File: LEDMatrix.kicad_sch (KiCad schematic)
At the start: 50 parts, among them J1 Conn_02x04_Odd_Even, SW2 SW_Push, U1 W25Q16JVUXIQ, U2 RP2040, Y1 12.000MHz

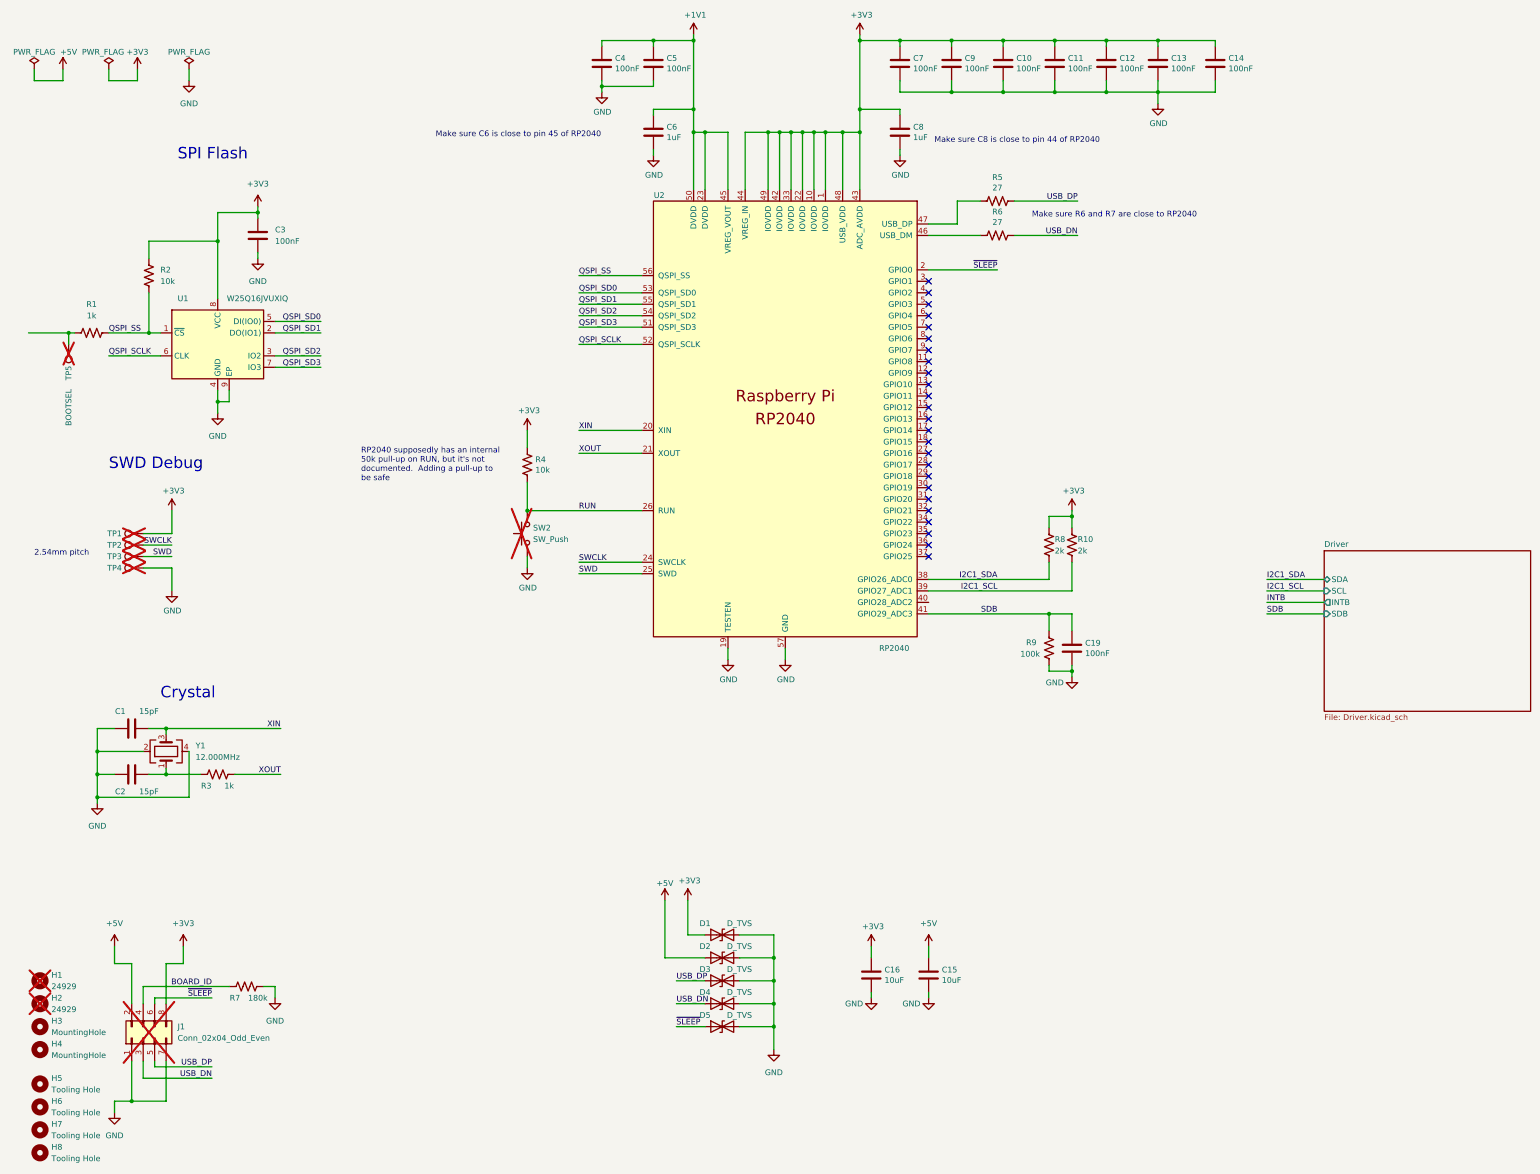
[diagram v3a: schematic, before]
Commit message: Version 2, with right angle neopixel backlighting
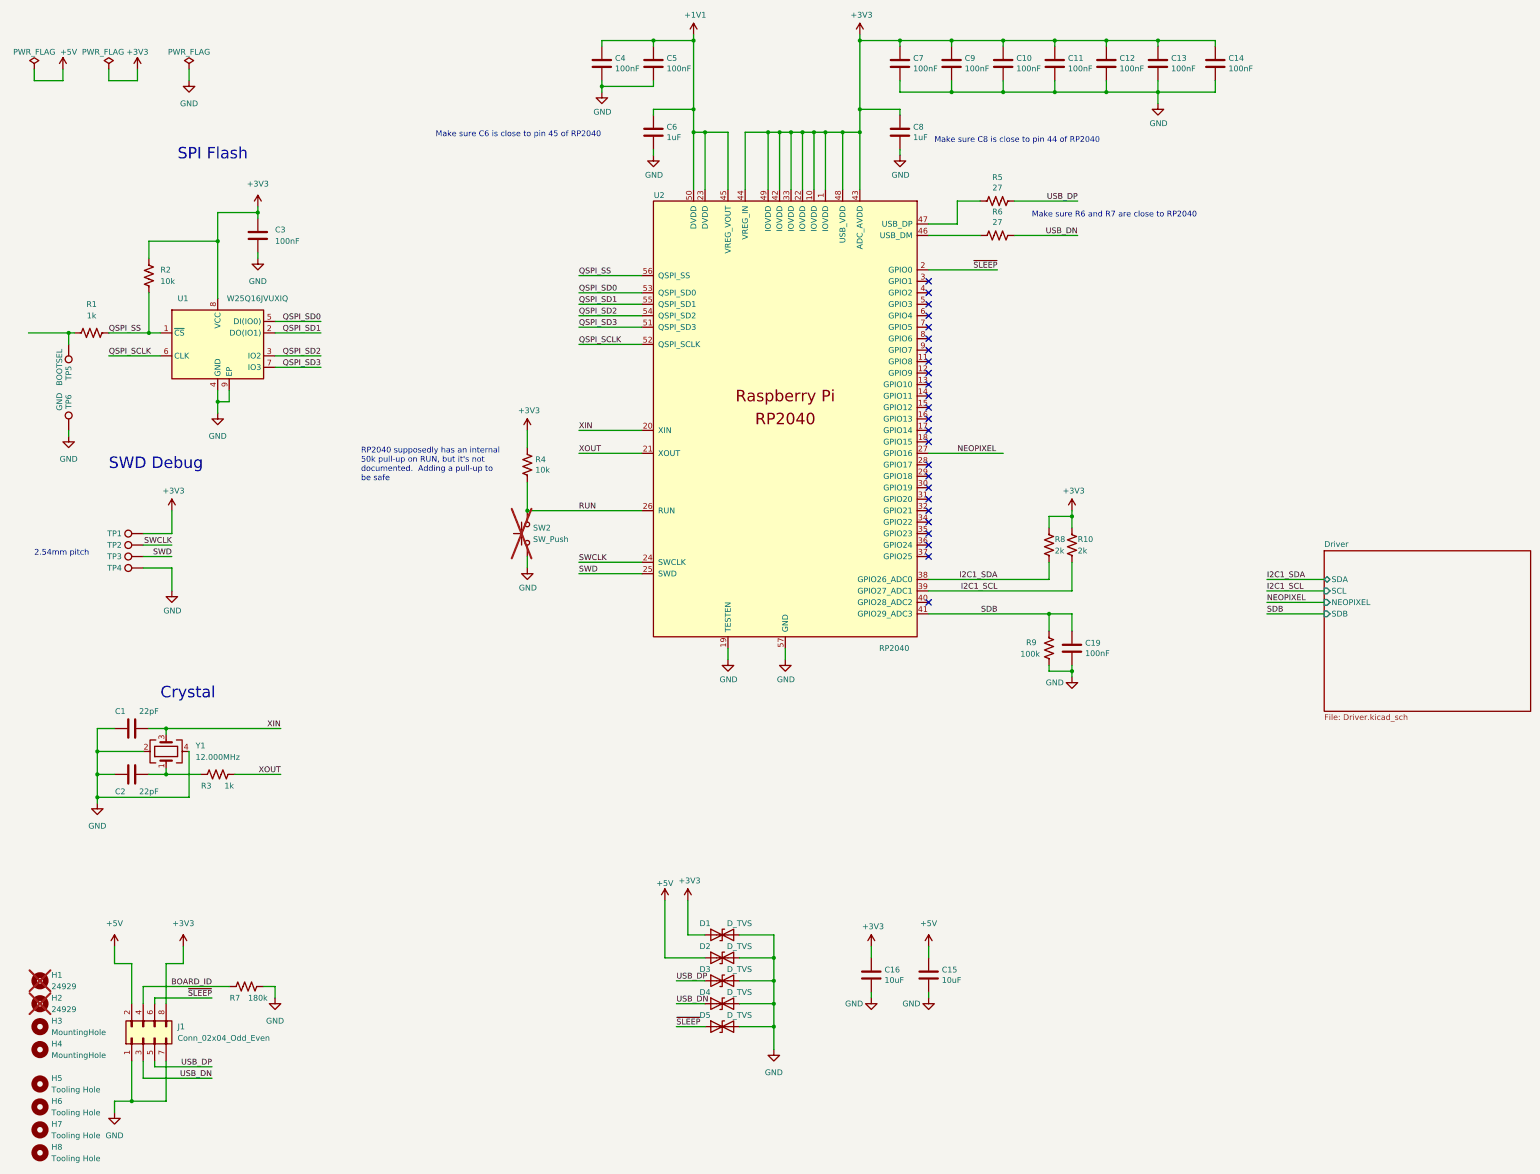
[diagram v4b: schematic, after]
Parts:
- added TP6: GND, TestPoint:TestPoint_Pad_D1.0mm, symbol Connector:TestPoint
- C1, C2: value 15pF -> 22pF
- J1, TP5: now fitted
- TP1, TP2, TP3, TP4: now fitted; now left out of the parts list
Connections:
- net GND: now also TP6.1
- net NEOPIXEL: now reaches U2.27 (GPIO16)
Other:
- sheet Driver ports: added NEOPIXEL; removed INTB
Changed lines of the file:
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@@
 	)
 	(no_connect
-		(at 224.79 113.03)
-	)
-	(no_connect
 		(at 224.79 92.71)
 	)
@@
 		(at 224.79 87.63)
 	)
+	(no_connect
+		(at 224.79 146.05)
+	)
 	(wire
 		(pts
@@
 	(wire
 		(pts
+			(xy 34.29 107.95) (xy 34.29 109.22)
+		)
+		(stroke
+			(width 0)
+			(type default)
+		)
+	)
+	(wire
+		(pts
 			(xy 161.29 113.03) (xy 147.32 113.03)
 		)
@@
 	(wire
 		(pts
+			(xy 299.72 146.05) (xy 312.42 146.05)
+		)
+		(stroke
+			(width 0)
+			(type default)
+		)
+	)
+	(wire
+		(pts
 			(xy 50.8 231.14) (xy 69.85 231.14)
 		)
@@
 	(wire
 		(pts
+			(xy 224.79 113.03) (xy 241.3 113.03)
+		)
+		(stroke
+			(width 0)
+			(type default)
+		)
+	)
+	(wire
+		(pts
 			(xy 50.8 133.35) (xy 57.15 133.35)
 		)
@@
 	(wire
 		(pts
-			(xy 299.72 146.05) (xy 312.42 146.05)
-		)
-		(stroke
-			(width 0)
-			(type default)
-		)
-	)
-	(wire
-		(pts
 			(xy 52.07 86.36) (xy 54.61 86.36)
 		)
@@
 		)
 	)
-	(label "INTB"
+	(label "NEOPIXEL"
 		(at 299.72 146.05 0)
 		(fields_autoplaced yes)
@@
 		)
 	)
+	(label "NEOPIXEL"
+		(at 231.14 113.03 0)
+		(fields_autoplaced yes)
+		(effects
+			(font
+				(size 1.27 1.27)
+			)
+			(justify left bottom)
+		)
+	)
 	(label "XOUT"
 		(at 147.32 113.03 0)
@@
 	)
 	(symbol
+		(lib_id "power:GND")
+		(at 34.29 109.22 0)
+		(unit 1)
+		(exclude_from_sim no)
+		(in_bom yes)
+		(on_board yes)
+		(dnp no)
+		(fields_autoplaced yes)
+		(property "Reference" "#PWR050"
+			(at 34.29 115.57 0)
+			(effects
+				(font
+					(size 1.27 1.27)
+				)
+				(hide yes)
+			)
+		)
+		(property "Value" "GND"
+			(at 34.29 114.3 0)
+			(effects
+				(font
+					(size 1.27 1.27)
+				)
+			)
+		)
+		(property "Footprint" ""
+			(at 34.29 109.22 0)
+			(effects
+				(font
+					(size 1.27 1.27)
+				)
+				(hide yes)
+			)
+		)
+		(property "Datasheet" ""
+			(at 34.29 109.22 0)
+			(effects
+				(font
+					(size 1.27 1.27)
+				)
+				(hide yes)
+			)
+		)
+		(property "Description" "Power symbol creates a global label with name \"GND\" , ground"
+			(at 34.29 109.22 0)
+			(effects
+				(font
+					(size 1.27 1.27)
+				)
+				(hide yes)
+			)
+		)
+		(pin "1"
+		)
+		(instances
+			(project "LEDMatrix"
+				(path "/2fa7b4ce-e682-4c2e-9419-b1318fe8c56d"
+					(reference "#PWR050")
+					(unit 1)
+				)
+			)
+		)
+	)
+	(symbol
 		(lib_id "Device:D_TVS")
 		(at 179.07 229.87 0)
@@
 		(unit 1)
 		(exclude_from_sim no)
-		(in_bom yes)
+		(in_bom no)
 		(on_board yes)
-		(dnp yes)
+		(dnp no)
 		(property "Reference" "TP1"
 			(at 44.45 130.81 90)
@@
 			)
 		)
-		(property "Value" "15pF"
+		(property "Value" "22pF"
 			(at 52.07 170.18 90)
 			(effects
@@
 		(in_bom no)
 		(on_board yes)
-		(dnp yes)
+		(dnp no)
 		(property "Reference" "TP5"
 			(at 34.29 95.25 90)
@@
 		)
 		(property "Value" "BOOTSEL"
-			(at 34.29 102.87 90)
+			(at 32.258 93.98 90)
 			(effects
 				(font
@@
 	)
 	(symbol
+		(lib_id "Connector:TestPoint")
+		(at 34.29 107.95 0)
+		(unit 1)
+		(exclude_from_sim no)
+		(in_bom no)
+		(on_board yes)
+		(dnp no)
+		(property "Reference" "TP6"
+			(at 34.29 101.6 90)
+			(effects
+				(font
+					(size 1.27 1.27)
+				)
+			)
+		)
+		(property "Value" "GND"
+			(at 32.258 101.6 90)
+			(effects
+				(font
+					(size 1.27 1.27)
+				)
+			)
+		)
+		(property "Footprint" "TestPoint:TestPoint_Pad_D1.0mm"
+			(at 39.37 107.95 0)
+			(effects
+				(font
+					(size 1.27 1.27)
+				)
+				(hide yes)
+			)
+		)
+		(property "Datasheet" "~"
+			(at 39.37 107.95 0)
+			(effects
+				(font
+					(size 1.27 1.27)
+				)
+				(hide yes)
+			)
+		)
+		(property "Description" "test point"
+			(at 34.29 107.95 0)
+			(effects
+				(font
+					(size 1.27 1.27)
+				)
+				(hide yes)
+			)
+		)
+		(property "LCSC" ""
+			(at 34.29 107.95 0)
+			(effects
+				(font
+					(size 1.27 1.27)
+				)
+				(hide yes)
+			)
+		)
+		(property "Digikey" ""
+			(at 34.29 107.95 0)
+			(effects
+				(font
+					(size 1.27 1.27)
+				)
+				(hide yes)
+			)
+		)
+		(property "LCSC Alt" ""
+			(at 34.29 107.95 0)
+			(effects
+				(font
+					(size 1.27 1.27)
+				)
+				(hide yes)
+			)
+		)
+		(pin "1"
+		)
+		(instances
+			(project "LEDMatrix"
+				(path "/2fa7b4ce-e682-4c2e-9419-b1318fe8c56d"
+					(reference "TP6")
+					(unit 1)
+				)
+			)
+		)
+	)
+	(symbol
 		(lib_id "power:GND")
 		(at 76.2 69.85 0)
@@
 		(unit 1)
 		(exclude_from_sim no)
-		(in_bom yes)
+		(in_bom no)
 		(on_board yes)
-		(dnp yes)
+		(dnp no)
 		(property "Reference" "TP2"
 			(at 44.45 133.35 90)
@@
 			)
 		)
-		(property "Value" "15pF"
+		(property "Value" "22pF"
 			(at 52.07 187.96 90)
 			(effects
@@
 		(unit 1)
 		(exclude_from_sim no)
-		(in_bom yes)
+		(in_bom no)
 		(on_board yes)
-		(dnp yes)
+		(dnp no)
 		(property "Reference" "TP4"
 			(at 44.45 138.43 90)
@@
 		(in_bom no)
 		(on_board yes)
-		(dnp yes)
+		(dnp no)
 		(fields_autoplaced yes)
 		(property "Reference" "J1"
@@
 		(unit 1)
 		(exclude_from_sim no)
-		(in_bom yes)
+		(in_bom no)
 		(on_board yes)
-		(dnp yes)
+		(dnp no)
 		(property "Reference" "TP3"
 			(at 44.45 135.89 90)
@@
 			)
 		)
-		(pin "INTB" output
-			(at 312.42 146.05 180)
+		(pin "SDB" input
+			(at 312.42 148.59 180)
 			(effects
 				(font
@@
 			)
 		)
-		(pin "SDB" input
-			(at 312.42 148.59 180)
+		(pin "NEOPIXEL" input
+			(at 312.42 146.05 180)
 			(effects
 				(font

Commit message: Another update before sending to JLCPCB
1. Narrowed the spacing between the LED displays
2. Made the position of the neopixels more consistent
3. Extended the silkscreen up a bit
4. Added my name to the front of the board
5. Designed the enclosure grid
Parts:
- U1, U2: JLCPCB Rotation Offset (none) -> -90

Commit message: Update 3d models
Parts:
- H1, H2: now fitted
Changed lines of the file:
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@@
 		(in_bom yes)
 		(on_board yes)
-		(dnp yes)
+		(dnp no)
 		(property "Reference" "H2"
 			(at 30.48 233.68 0)
@@
 		(in_bom yes)
 		(on_board yes)
-		(dnp yes)
+		(dnp no)
 		(property "Reference" "H1"
 			(at 30.48 228.6 0)
